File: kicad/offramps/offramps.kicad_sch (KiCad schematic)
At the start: 205 parts, among them J10 Conn_01x04_Socket, J11 Screw_Terminal_01x02, J12 Conn_01x04_Pin, J13 Micro_SD_Card, J14 Conn_01x03_Male, J15 Screw_Terminal_01x02, J16 Conn_01x02_Pin, J17 Conn_01x02_Pin, J3 VITA_57.1_FMC_HPC_Carrier, J4 Conn_01x02_Pin, J5 Conn_Coaxial, J6 Conn_01x03_Male, J7 Conn_Coaxial, J8 Conn_Coaxial, J9 Conn_01x06_Male, Q1 BSS138, Q10 BSS138, Q11 BSS138, Q12 BSS138, Q13 NPN, Q14 NPN, Q15 NPN, Q16 NPN, Q17 BSS138, Q2 BSS138, Q25 BSS138, Q26 BSS138, Q27 BSS138, Q28 BSS138, Q29 BSS138, Q3 BSS138, Q30 BSS138, Q4 BSS138, Q5 BSS138, Q6 BSS138, Q7 BSS138, Q8 BSS138, Q9 BSS138, SW1 219-8MST, U1 TXB0108PWR, U10 MCP4725xxx-xCH, U11 LMH6611MK/NOPB, U12 ADC1173CIMTC/NOPB, U13 MCP4725xxx-xCH, U14 POPA2994IDGKR, U15 ADS1114IDGS, U16 LIS2MDLTR, U17 LSM6DSRTR, U18 LTC-4627JR, U19 AMS1117-3.3, U2 TXB0108PWR, U3 TXB0108PWR, U4 TXB0108PWR, U5 TXB0108PWR, U6 LMH6611MK/NOPB, U7 ADC1175CIMTC/NOPB, U8 TXB0108PWR, U9 PTMUX4053PWR

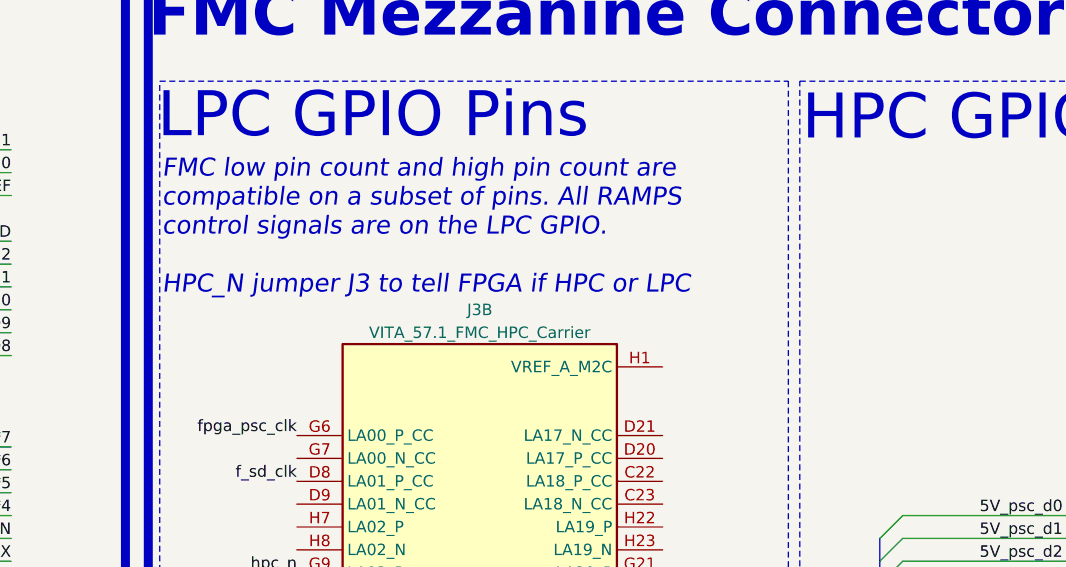
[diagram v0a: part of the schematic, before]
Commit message: Most components placed, need to re-arrange LPC pins for routing
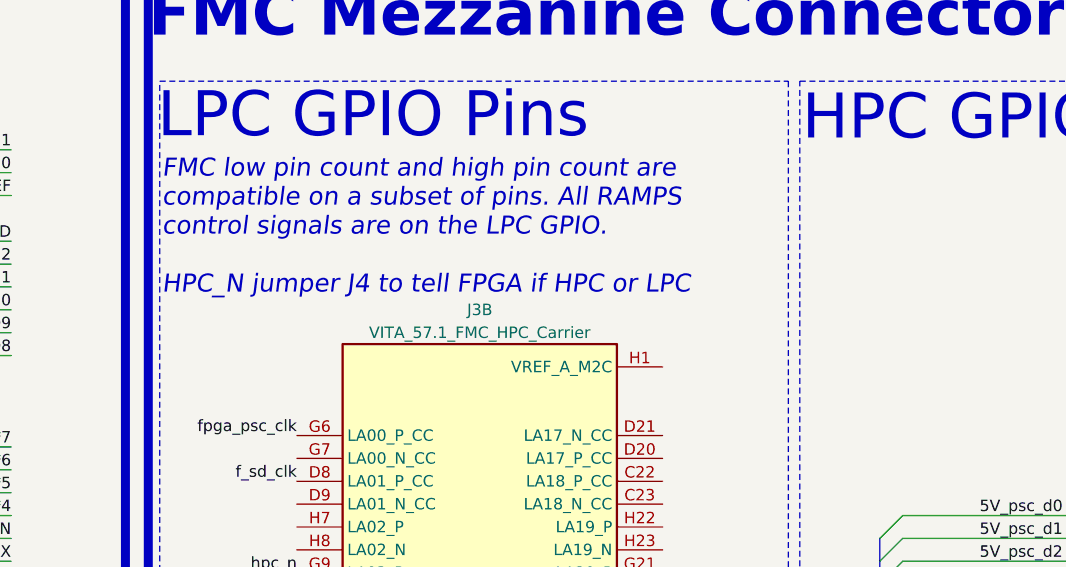
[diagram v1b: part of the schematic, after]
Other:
- note added: "FMC low pin count and high pin count are compatible on a subset of pins. All RAMPS control signals are on the LPC GPIO. HPC_N jumper J4 to tell FPGA if HPC or LPC"
- note removed: "FMC low pin count and high pin count are compatible on a subset of pins. All RAMPS control signals are on the LPC GPIO. HPC_N jumper J3 to tell FPGA if HPC or LPC"
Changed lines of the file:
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@@
 		)
 	)
-	(text "FMC low pin count and high pin count are\ncompatible on a subset of pins. All RAMPS\ncontrol signals are on the LPC GPIO.\n\nHPC_N jumper J3 to tell FPGA if HPC or LPC"
+	(text "FMC low pin count and high pin count are\ncompatible on a subset of pins. All RAMPS\ncontrol signals are on the LPC GPIO.\n\nHPC_N jumper J4 to tell FPGA if HPC or LPC"
 		(exclude_from_sim no)
 		(at 184.404 44.196 0)

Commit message: Update: Continued Routing
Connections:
- net f_sd_cmd: now also J3.C22 (LA18_P_CC); no longer J3.E10 (HA09_N)
- net f_sd_dat0: now also J3.H22 (LA19_P); no longer J3.K14 (HA10_N)
- net f_sd_dat1: now also J3.C23 (LA18_N_CC); no longer J3.K13 (HA10_P)
- net f_sd_dat2: now also J3.G21 (LA20_P); no longer J3.J13 (HA11_N)
- net f_sd_dat3: now also J3.H23 (LA19_N); no longer J3.J12 (HA11_P)
- net ls_f_E1-DIR: now also J3.H25 (LA21_P); no longer J3.H35 (LA30_N)
- net ls_f_E1-STEP: now also J3.G22 (LA20_N); no longer J3.G33 (LA31_P)
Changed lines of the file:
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@@
 	)
 	(label "f_sd_dat3"
-		(at 285.75 104.14 180)
+		(at 240.03 80.01 0)
 		(fields_autoplaced yes)
 		(effects
@@
 				(size 1.27 1.27)
 			)
-			(justify right bottom)
+			(justify left bottom)
 		)
 	)
@@
 	)
 	(label "ls_f_E1-STEP"
-		(at 240.03 138.43 0)
+		(at 240.03 85.09 0)
 		(fields_autoplaced yes)
 		(effects
@@
 	)
 	(label "f_sd_dat1"
-		(at 285.75 99.06 180)
+		(at 240.03 74.93 0)
 		(fields_autoplaced yes)
 		(effects
@@
 				(size 1.27 1.27)
 			)
-			(justify right bottom)
+			(justify left bottom)
 		)
 	)
@@
 	)
 	(label "f_sd_dat0"
-		(at 285.75 101.6 180)
+		(at 240.03 77.47 0)
 		(fields_autoplaced yes)
 		(effects
@@
 				(size 1.27 1.27)
 			)
-			(justify right bottom)
+			(justify left bottom)
 		)
 	)
@@
 	)
 	(label "ls_f_E1-DIR"
-		(at 240.03 135.89 0)
+		(at 240.03 87.63 0)
 		(fields_autoplaced yes)
 		(effects
@@
 	)
 	(label "f_sd_dat2"
-		(at 285.75 106.68 180)
+		(at 240.03 82.55 0)
 		(fields_autoplaced yes)
 		(effects
@@
 				(size 1.27 1.27)
 			)
-			(justify right bottom)
+			(justify left bottom)
 		)
 	)
@@
 	)
 	(label "f_sd_cmd"
-		(at 285.75 96.52 180)
+		(at 240.03 72.39 0)
 		(fields_autoplaced yes)
 		(effects
@@
 				(size 1.27 1.27)
 			)
-			(justify right bottom)
+			(justify left bottom)
 		)
 	)

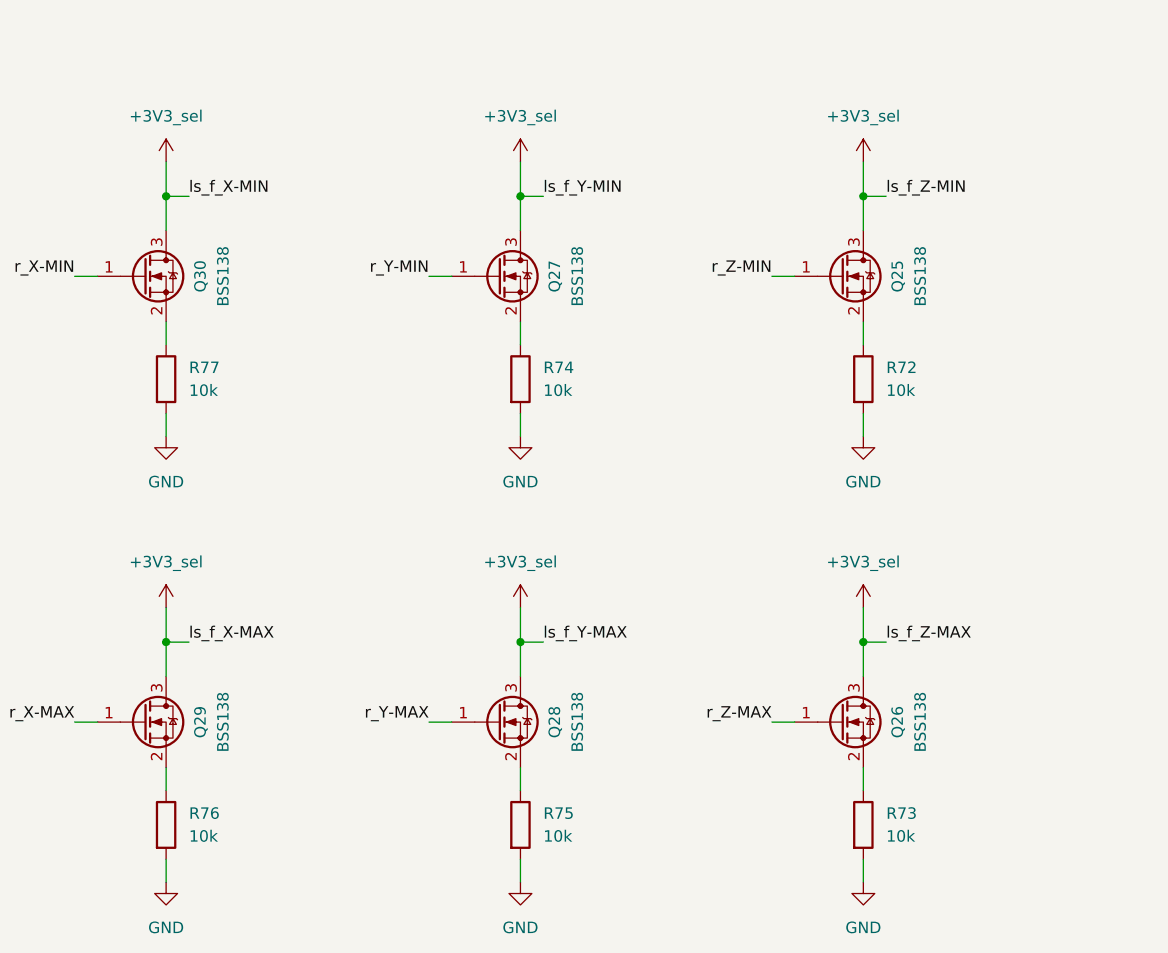
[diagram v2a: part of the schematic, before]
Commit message: Routing Updates ~150 traces left
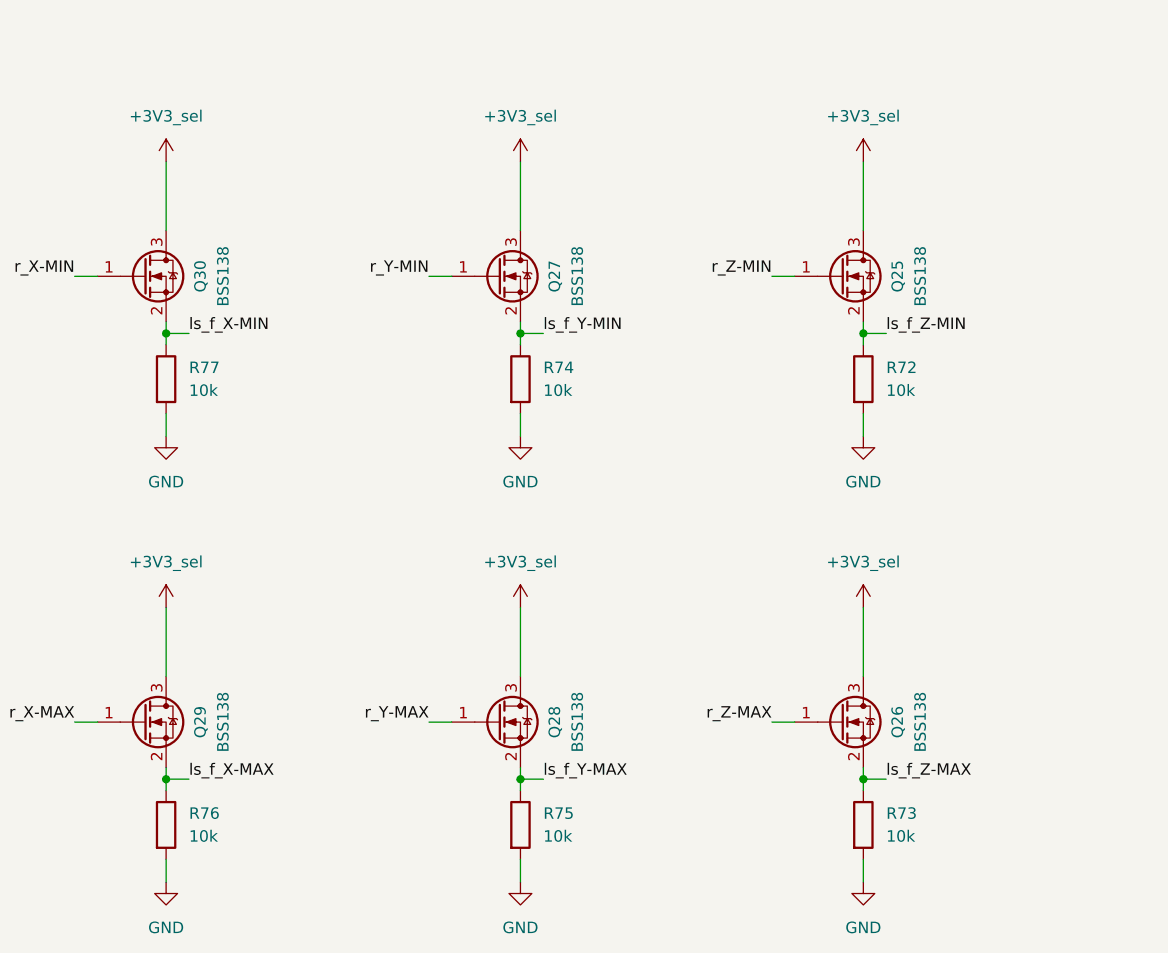
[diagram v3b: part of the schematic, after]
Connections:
- net +3V3_sel: no longer J3.G19 (LA16_N), J3.G34 (LA31_N), J3.G36 (LA33_P), J3.G37 (LA33_N), J3.H37 (LA32_P), J3.H38 (LA32_N), Q1.3 (D), Q2.3 (D), Q3.3 (D), Q4.3 (D), Q5.3 (D), Q6.3 (D), R2.1, R3.1, R5.1, R6.1, R8.1, R9.1
- net ls_f_Y-MIN: now reaches Q27.2 (S), R74.1
- net ls_f_Y-MIN: now also J3.H37 (LA32_P), Q3.3 (D), R5.1
- net ls_f_Z-MAX: now reaches Q26.2 (S), R73.1
- net ls_f_Z-MAX: now also J3.G19 (LA16_N), Q6.3 (D), R9.1
- net ls_f_Y-MAX: now reaches Q28.2 (S), R75.1
- net ls_f_Y-MAX: now also J3.G37 (LA33_N), Q4.3 (D), R6.1
- net ls_f_Z-MIN: now reaches Q25.2 (S), R72.1
- net ls_f_Z-MIN: now also J3.H38 (LA32_N), Q5.3 (D), R8.1
- net ls_f_X-MAX: now reaches Q29.2 (S), R76.1
- net ls_f_X-MAX: now also J3.G36 (LA33_P), Q2.3 (D), R3.1
- net ls_f_X-MIN: now reaches Q30.2 (S), R77.1
- net ls_f_X-MIN: now also J3.G34 (LA31_N), Q1.3 (D), R2.1
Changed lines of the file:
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@@
 	)
 	(junction
-		(at 124.46 429.26)
-		(diameter 0)
-		(color 0 0 0 0)
-	)
-	(junction
 		(at 645.16 59.69)
 		(diameter 0)
@@
 	)
 	(junction
-		(at 86.36 379.73)
+		(at 124.46 394.97)
 		(diameter 0)
 		(color 0 0 0 0)
@@
 	)
 	(junction
-		(at 124.46 379.73)
-		(diameter 0)
-		(color 0 0 0 0)
-	)
-	(junction
 		(at 558.8 78.74)
 		(diameter 0)
@@
 	)
 	(junction
+		(at 46.99 444.5)
+		(diameter 0)
+		(color 0 0 0 0)
+	)
+	(junction
 		(at 543.56 43.18)
 		(diameter 0)
@@
 	)
 	(junction
-		(at 584.2 288.29)
+		(at 86.36 444.5)
 		(diameter 0)
 		(color 0 0 0 0)
 	)
 	(junction
-		(at 86.36 429.26)
+		(at 584.2 288.29)
 		(diameter 0)
 		(color 0 0 0 0)
@@
 	)
 	(junction
+		(at 86.36 394.97)
+		(diameter 0)
+		(color 0 0 0 0)
+	)
+	(junction
 		(at 579.12 351.79)
 		(diameter 0)
@@
 	)
 	(junction
+		(at 124.46 444.5)
+		(diameter 0)
+		(color 0 0 0 0)
+	)
+	(junction
 		(at 560.07 118.11)
 		(diameter 0)
@@
 	)
 	(junction
+		(at 46.99 394.97)
+		(diameter 0)
+		(color 0 0 0 0)
+	)
+	(junction
 		(at 208.28 226.06)
 		(diameter 0)
@@
 	)
 	(junction
-		(at 46.99 379.73)
-		(diameter 0)
-		(color 0 0 0 0)
-	)
-	(junction
 		(at 591.82 356.87)
 		(diameter 0)
@@
 		(color 0 0 0 0)
 	)
-	(junction
-		(at 46.99 429.26)
-		(diameter 0)
-		(color 0 0 0 0)
-	)
 	(no_connect
 		(at 553.72 271.78)
@@
 	(wire
 		(pts
-			(xy 86.36 375.92) (xy 86.36 379.73)
-		)
-		(stroke
-			(width 0)
-			(type default)
-		)
-	)
-	(wire
-		(pts
 			(xy 571.5 233.68) (xy 574.04 233.68)
 		)
@@
 	(wire
 		(pts
-			(xy 46.99 383.54) (xy 46.99 379.73)
-		)
-		(stroke
-			(width 0)
-			(type default)
-		)
-	)
-	(wire
-		(pts
 			(xy 514.35 408.94) (xy 516.89 408.94)
 		)
@@
 	(wire
 		(pts
-			(xy 46.99 375.92) (xy 46.99 379.73)
+			(xy 46.99 375.92) (xy 46.99 383.54)
 		)
 		(stroke
@@
 	(wire
 		(pts
-			(xy 124.46 429.26) (xy 127 429.26)
+			(xy 124.46 444.5) (xy 127 444.5)
 		)
 		(stroke
@@
 	(wire
 		(pts
-			(xy 86.36 425.45) (xy 86.36 429.26)
-		)
-		(stroke
-			(width 0)
-			(type default)
-		)
-	)
-	(wire
-		(pts
 			(xy 40.64 119.38) (xy 40.64 129.54)
 		)
@@
 	(wire
 		(pts
-			(xy 86.36 443.23) (xy 86.36 445.77)
+			(xy 86.36 443.23) (xy 86.36 444.5)
 		)
 		(stroke
@@
 	(wire
 		(pts
-			(xy 46.99 425.45) (xy 46.99 429.26)
-		)
-		(stroke
-			(width 0)
-			(type default)
-		)
-	)
-	(wire
-		(pts
 			(xy 591.82 231.14) (xy 591.82 232.41)
 		)
@@
 	(wire
 		(pts
-			(xy 86.36 379.73) (xy 88.9 379.73)
+			(xy 86.36 394.97) (xy 88.9 394.97)
 		)
 		(stroke
@@
 	(wire
 		(pts
-			(xy 86.36 429.26) (xy 86.36 433.07)
+			(xy 86.36 425.45) (xy 86.36 433.07)
 		)
 		(stroke
@@
 	(wire
 		(pts
-			(xy 124.46 393.7) (xy 124.46 396.24)
+			(xy 124.46 393.7) (xy 124.46 394.97)
 		)
 		(stroke
@@
 	(wire
 		(pts
-			(xy 46.99 443.23) (xy 46.99 445.77)
+			(xy 46.99 443.23) (xy 46.99 444.5)
 		)
 		(stroke
@@
 	(wire
 		(pts
+			(xy 86.36 444.5) (xy 86.36 445.77)
+		)
+		(stroke
+			(width 0)
+			(type default)
+		)
+	)
+	(wire
+		(pts
 			(xy 471.17 405.13) (xy 477.52 405.13)
 		)
@@
 	(wire
 		(pts
-			(xy 46.99 429.26) (xy 46.99 433.07)
+			(xy 46.99 425.45) (xy 46.99 433.07)
 		)
 		(stroke
@@
 	(wire
 		(pts
-			(xy 86.36 379.73) (xy 86.36 383.54)
+			(xy 86.36 375.92) (xy 86.36 383.54)
 		)
 		(stroke
@@
 	(wire
 		(pts
-			(xy 124.46 379.73) (xy 127 379.73)
+			(xy 124.46 394.97) (xy 127 394.97)
 		)
 		(stroke
@@
 		)
 	)
+	(wire
+		(pts
+			(xy 86.36 394.97) (xy 86.36 396.24)
+		)
+		(stroke
+			(width 0)
+			(type default)
+		)
+	)
 	(bus
 		(pts
@@
 	(wire
 		(pts
-			(xy 86.36 393.7) (xy 86.36 396.24)
-		)
-		(stroke
-			(width 0)
-			(type default)
-		)
-	)
-	(wire
-		(pts
-			(xy 124.46 379.73) (xy 124.46 383.54)
+			(xy 86.36 393.7) (xy 86.36 394.97)
 		)
 		(stroke
@@
 	(wire
 		(pts
-			(xy 124.46 429.26) (xy 124.46 433.07)
+			(xy 124.46 425.45) (xy 124.46 433.07)
 		)
 		(stroke
@@
 	(wire
 		(pts
-			(xy 124.46 425.45) (xy 124.46 429.26)
-		)
-		(stroke
-			(width 0)
-			(type default)
-		)
-	)
-	(wire
-		(pts
 			(xy 209.55 410.21) (xy 209.55 401.32)
 		)
@@
 	(wire
 		(pts
-			(xy 46.99 393.7) (xy 46.99 396.24)
+			(xy 46.99 393.7) (xy 46.99 394.97)
 		)
 		(stroke
@@
 	(wire
 		(pts
-			(xy 46.99 429.26) (xy 49.53 429.26)
+			(xy 46.99 444.5) (xy 49.53 444.5)
 		)
 		(stroke
@@
 	(wire
 		(pts
+			(xy 124.46 444.5) (xy 124.46 445.77)
+		)
+		(stroke
+			(width 0)
+			(type default)
+		)
+	)
+	(wire
+		(pts
 			(xy 406.4 382.27) (xy 406.4 384.81)
 		)
@@
 	(wire
 		(pts
-			(xy 46.99 379.73) (xy 49.53 379.73)
+			(xy 46.99 394.97) (xy 49.53 394.97)
 		)
 		(stroke
@@
 	(wire
 		(pts
-			(xy 124.46 443.23) (xy 124.46 445.77)
+			(xy 124.46 443.23) (xy 124.46 444.5)
 		)
 		(stroke
@@
 	(wire
 		(pts
+			(xy 46.99 444.5) (xy 46.99 445.77)
+		)
+		(stroke
+			(width 0)
+			(type default)
+		)
+	)
+	(wire
+		(pts
 			(xy 266.7 356.87) (xy 281.94 356.87)
 		)
@@
 	(wire
 		(pts
-			(xy 86.36 429.26) (xy 88.9 429.26)
+			(xy 86.36 444.5) (xy 88.9 444.5)
 		)
 		(stroke
@@
 	(wire
 		(pts
-			(xy 124.46 375.92) (xy 124.46 379.73)
+			(xy 124.46 375.92) (xy 124.46 383.54)
 		)
 		(stroke
@@
 	(wire
 		(pts
+			(xy 124.46 394.97) (xy 124.46 396.24)
+		)
+		(stroke
+			(width 0)
+			(type default)
+		)
+	)
+	(wire
+		(pts
 			(xy 496.57 346.71) (xy 515.62 346.71)
 		)
@@
 		)
 	)
+	(wire
+		(pts
+			(xy 46.99 394.97) (xy 46.99 396.24)
+		)
+		(stroke
+			(width 0)
+			(type default)
+		)
+	)
 	(bus
 		(pts
@@
 	)
 	(label "ls_f_Z-MIN"
-		(at 127 379.73 0)
+		(at 127 394.97 0)
 		(fields_autoplaced yes)
 		(effects
@@
 	)
 	(label "ls_f_Z-MAX"
-		(at 127 429.26 0)
+		(at 127 444.5 0)
 		(fields_autoplaced yes)
 		(effects
@@
 	)
 	(label "ls_f_X-MAX"
-		(at 49.53 429.26 0)
+		(at 49.53 444.5 0)
 		(fields_autoplaced yes)
 		(effects
@@
 	)
 	(label "ls_f_Y-MAX"
-		(at 88.9 429.26 0)
+		(at 88.9 444.5 0)
 		(fields_autoplaced yes)
 		(effects
@@
 	)
 	(label "ls_f_X-MIN"
-		(at 49.53 379.73 0)
+		(at 49.53 394.97 0)
 		(fields_autoplaced yes)
 		(effects
@@
 	)
 	(label "ls_f_Y-MIN"
-		(at 88.9 379.73 0)
+		(at 88.9 394.97 0)
 		(fields_autoplaced yes)
 		(effects

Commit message: Fixed some labeling issues and re-added an opamp that disappeared
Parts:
- added JP28: Jumper_3_Open, Connector_PinHeader_2.54mm:PinHeader_1x03_P2.54mm_Vertical, symbol Jumper:Jumper_3_Open
- added R4, R50: 10k, Resistor_SMD:R_0805_2012Metric, symbol Device:R
- added R51, R55: 5k, Resistor_SMD:R_0805_2012Metric, symbol Device:R
- added U20: LM358DR2G, external_footprints:SOIC127P599X175-8N, symbol LM358DR:LM358DR
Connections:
- net f_dac_THERM0-SCL is gone; now on net fpga_SCL: U10.5 (SCL)
- net f_dac_THERM0-SDA is gone; now on net fpga_SDA: U10.4 (SDA)
- net f_dac_THERM1-SCL is gone; now on net fpga_SCL: U13.5 (SCL)
- net f_dac_THERM1-SDA is gone; now on net fpga_SDA: U13.4 (SDA)
- net u_LED is gone; now on net u_r_LED: J1.82 (~D13)
- net +5V_sel: now also U20.8 (VCC)
- net 7seg_A1: now also J3.E10 (HA09_N)
- net 7seg_A2: now also J3.K13 (HA10_P)
- net 7seg_A3: now also J3.K14 (HA10_N)
- net 7seg_A4: now also J3.J12 (HA11_P)
- net GND: now also R4.1, R50.1, U20.4 (GND)
- net dac_op_THERM0: now also U20.3 (1IN+)
- net dac_op_THERM1: now also U20.5 (2IN+)
- net ls_jump_E1-EN: now also JP28.3 (B)
- net op_mux_THERM0: now also R55.2, U20.1 (1OUT)
- net op_mux_THERM1: now also R51.2, U20.7 (2OUT)
- net r_E1-DIR: now also J2.45 (D34)
- net r_E1-STEP: now also J2.43 (D36)
- net u_E1-DIR: now also J1.45 (D34)
- net u_E1-EN: now also J1.49 (D30), JP28.1 (A)
- net u_E1-STEP: now also J1.43 (D36)
- removed net E1-DIR: J1.45 (D34), J2.45 (D34)
- net E1-EN renamed r_E1-EN
- net r_E1-EN: now also JP28.2 (C); no longer J1.49 (D30)
- removed net E1-STEP: J1.43 (D36), J2.43 (D36)
- net r_LED renamed u_r_LED
- new net: R50.2, R55.1, U20.2 (1IN-)
- new net: R4.2, R51.1, U20.6 (2IN-)
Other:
- moved on the sheet: C23, C24, C37, C39, R32, R33, R39, R40, R47, R48, U10, U13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
